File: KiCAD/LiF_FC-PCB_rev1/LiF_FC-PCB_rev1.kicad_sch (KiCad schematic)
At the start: 0 parts

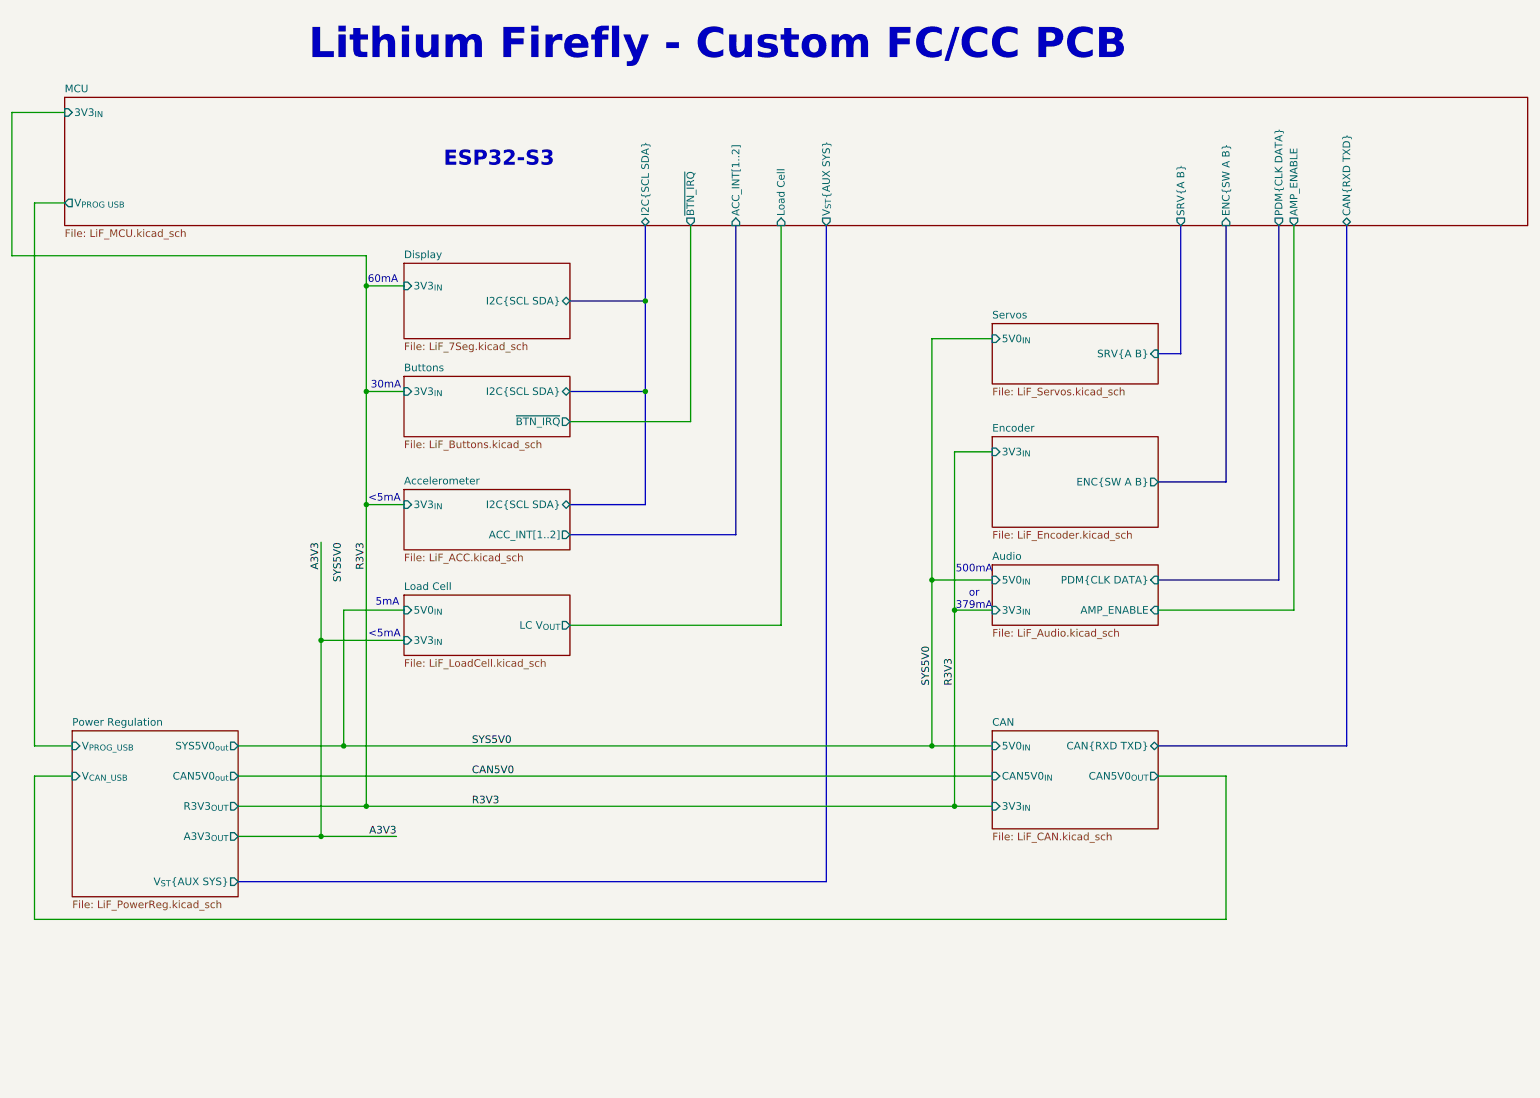
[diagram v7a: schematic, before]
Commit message: added door limit switch and fixed I2C pull up resistors
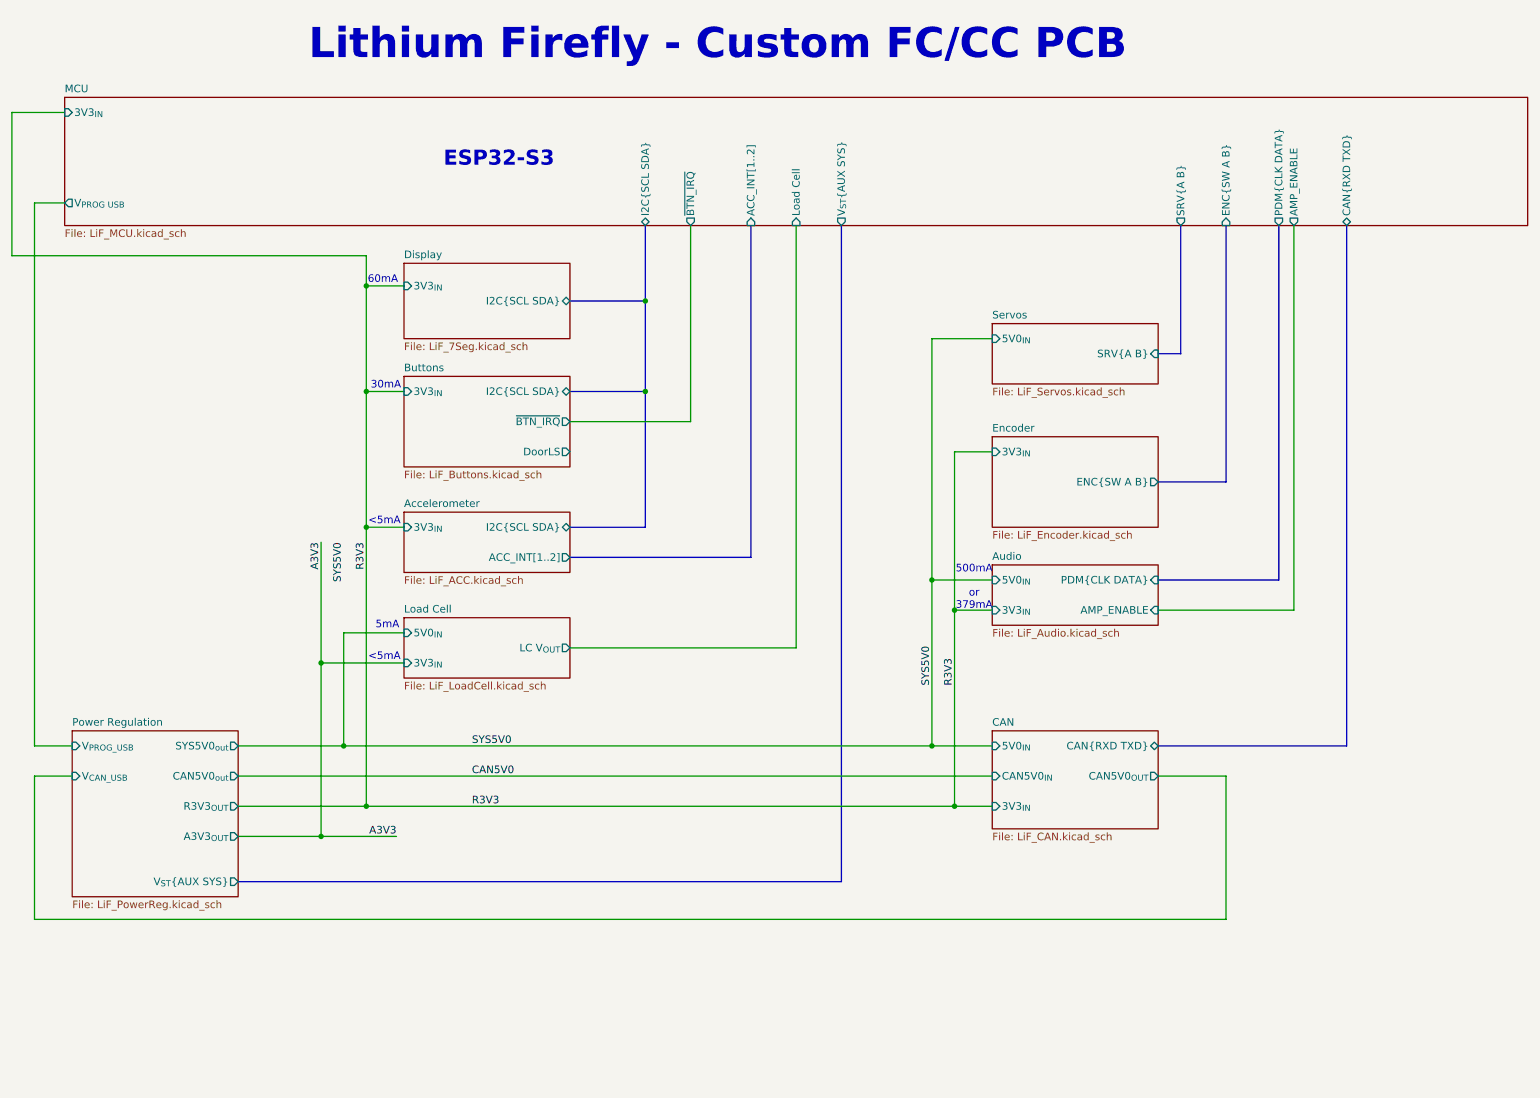
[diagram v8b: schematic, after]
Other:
- sheet Buttons ports: added DoorLS; removed none
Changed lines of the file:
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@@
 	(text "<5mA"
 		(exclude_from_sim no)
-		(at 77.978 94.234 0)
+		(at 77.978 98.044 0)
 		(effects
 			(font
@@
 	(text "5mA"
 		(exclude_from_sim no)
-		(at 78.486 111.76 0)
+		(at 78.486 115.57 0)
 		(effects
 			(font
@@
 	(text "<5mA"
 		(exclude_from_sim no)
-		(at 77.978 117.094 0)
+		(at 77.978 120.904 0)
 		(effects
 			(font
@@
 	)
 	(junction
-		(at 67.31 118.11)
+		(at 74.93 99.06)
 		(diameter 0)
 		(color 0 0 0 0)
@@
 	)
 	(junction
-		(at 74.93 95.25)
-		(diameter 0)
-		(color 0 0 0 0)
-	)
-	(junction
 		(at 67.31 151.13)
 		(diameter 0)
@@
 		(color 0 0 0 0)
 	)
-	(wire
-		(pts
-			(xy 144.78 115.57) (xy 109.22 115.57)
+	(junction
+		(at 67.31 121.92)
+		(diameter 0)
+		(color 0 0 0 0)
+	)
+	(wire
+		(pts
+			(xy 147.32 119.38) (xy 109.22 119.38)
 		)
 		(stroke
@@
 		)
 	)
-	(wire
-		(pts
-			(xy 74.93 95.25) (xy 74.93 146.05)
-		)
-		(stroke
-			(width 0)
-			(type default)
-		)
-	)
 	(bus
 		(pts
@@
 	(bus
 		(pts
-			(xy 137.16 48.26) (xy 137.16 100.33)
-		)
-		(stroke
-			(width 0)
-			(type default)
-		)
-	)
-	(wire
-		(pts
-			(xy 74.93 95.25) (xy 81.28 95.25)
-		)
-		(stroke
-			(width 0)
-			(type default)
-		)
-	)
-	(bus
-		(pts
-			(xy 109.22 95.25) (xy 121.92 95.25)
-		)
-		(stroke
-			(width 0)
-			(type default)
-		)
-	)
-	(wire
-		(pts
-			(xy 74.93 76.2) (xy 74.93 95.25)
+			(xy 139.7 48.26) (xy 139.7 104.14)
+		)
+		(stroke
+			(width 0)
+			(type default)
+		)
+	)
+	(wire
+		(pts
+			(xy 74.93 99.06) (xy 81.28 99.06)
+		)
+		(stroke
+			(width 0)
+			(type default)
+		)
+	)
+	(bus
+		(pts
+			(xy 109.22 99.06) (xy 121.92 99.06)
 		)
 		(stroke
@@
 	(bus
 		(pts
-			(xy 152.4 158.75) (xy 53.34 158.75)
+			(xy 154.94 158.75) (xy 53.34 158.75)
 		)
 		(stroke
@@
 	(wire
 		(pts
-			(xy 71.12 113.03) (xy 81.28 113.03)
+			(xy 71.12 116.84) (xy 81.28 116.84)
 		)
 		(stroke
@@
 	(wire
 		(pts
-			(xy 144.78 48.26) (xy 144.78 115.57)
-		)
-		(stroke
-			(width 0)
-			(type default)
-		)
-	)
-	(bus
-		(pts
-			(xy 137.16 100.33) (xy 109.22 100.33)
+			(xy 147.32 48.26) (xy 147.32 119.38)
+		)
+		(stroke
+			(width 0)
+			(type default)
+		)
+	)
+	(bus
+		(pts
+			(xy 139.7 104.14) (xy 109.22 104.14)
 		)
 		(stroke
@@
 	(wire
 		(pts
-			(xy 67.31 118.11) (xy 67.31 151.13)
+			(xy 74.93 99.06) (xy 74.93 146.05)
 		)
 		(stroke
@@
 		)
 	)
+	(wire
+		(pts
+			(xy 74.93 76.2) (xy 74.93 99.06)
+		)
+		(stroke
+			(width 0)
+			(type default)
+		)
+	)
 	(bus
 		(pts
@@
 	(wire
 		(pts
-			(xy 67.31 101.6) (xy 67.31 118.11)
+			(xy 67.31 101.6) (xy 67.31 121.92)
 		)
 		(stroke
@@
 		)
 	)
+	(wire
+		(pts
+			(xy 67.31 121.92) (xy 67.31 151.13)
+		)
+		(stroke
+			(width 0)
+			(type default)
+		)
+	)
 	(bus
 		(pts
@@
 	(bus
 		(pts
-			(xy 152.4 48.26) (xy 152.4 158.75)
-		)
-		(stroke
-			(width 0)
-			(type default)
-		)
-	)
-	(bus
-		(pts
-			(xy 121.92 95.25) (xy 121.92 76.2)
-		)
-		(stroke
-			(width 0)
-			(type default)
-		)
-	)
-	(wire
-		(pts
-			(xy 67.31 118.11) (xy 81.28 118.11)
+			(xy 154.94 48.26) (xy 154.94 158.75)
+		)
+		(stroke
+			(width 0)
+			(type default)
+		)
+	)
+	(bus
+		(pts
+			(xy 121.92 99.06) (xy 121.92 76.2)
+		)
+		(stroke
+			(width 0)
+			(type default)
+		)
+	)
+	(wire
+		(pts
+			(xy 67.31 121.92) (xy 81.28 121.92)
 		)
 		(stroke
@@
 	(wire
 		(pts
-			(xy 71.12 113.03) (xy 71.12 135.89)
+			(xy 71.12 116.84) (xy 71.12 135.89)
 		)
 		(stroke
@@
 	)
 	(sheet
-		(at 81.28 110.49)
+		(at 81.28 114.3)
 		(size 27.94 10.16)
 		(exclude_from_sim no)
@@
 		)
 		(property "Sheetname" "Load Cell"
-			(at 81.28 109.7784 0)
+			(at 81.28 113.5884 0)
 			(effects
 				(font
@@
 		)
 		(property "Sheetfile" "LiF_LoadCell.kicad_sch"
-			(at 81.28 121.2346 0)
+			(at 81.28 125.0446 0)
 			(effects
 				(font
@@
 		)
 		(pin "3V3_{IN}" input
-			(at 81.28 118.11 180)
+			(at 81.28 121.92 180)
 			(effects
 				(font
@@
 		)
 		(pin "5V0_{IN}" input
-			(at 81.28 113.03 180)
+			(at 81.28 116.84 180)
 			(effects
 				(font
@@
 		)
 		(pin "LC V_{OUT}" output
-			(at 109.22 115.57 0)
+			(at 109.22 119.38 0)
 			(effects
 				(font
@@
 	)
 	(sheet
-		(at 81.28 92.71)
+		(at 81.28 96.52)
 		(size 27.94 10.16)
 		(exclude_from_sim no)
@@
 		)
 		(property "Sheetname" "Accelerometer"
-			(at 81.28 91.9984 0)
+			(at 81.28 95.8084 0)
 			(effects
 				(font
@@
 		)
 		(property "Sheetfile" "LiF_ACC.kicad_sch"
-			(at 81.28 103.4546 0)
+			(at 81.28 107.2646 0)
 			(effects
 				(font
@@
 		)
 		(pin "3V3_{IN}" input
-			(at 81.28 95.25 180)
+			(at 81.28 99.06 180)
 			(effects
 				(font
@@
 		)
 		(pin "ACC_INT[1..2]" output
-			(at 109.22 100.33 0)
+			(at 109.22 104.14 0)
 			(effects
 				(font
@@
 		)
 		(pin "I2C{SCL SDA}" bidirectional
-			(at 109.22 95.25 0)
+			(at 109.22 99.06 0)
 			(effects
 				(font
@@
 	(sheet
 		(at 81.28 73.66)
-		(size 27.94 10.16)
+		(size 27.94 15.24)
 		(exclude_from_sim no)
 		(in_bom yes)
@@
 		)
 		(property "Sheetfile" "LiF_Buttons.kicad_sch"
-			(at 81.28 84.4046 0)
+			(at 81.28 89.4846 0)
 			(effects
 				(font
@@
 		(pin "~{BTN_IRQ}" output
 			(at 109.22 81.28 0)
+			(effects
+				(font
+					(size 1.27 1.27)
+				)
+				(justify right)
+			)
+		)
+		(pin "DoorLS" output
+			(at 109.22 86.36 0)
 			(effects
 				(font
@@
 		)
 		(pin "ACC_INT[1..2]" input
-			(at 137.16 48.26 270)
+			(at 139.7 48.26 270)
 			(effects
 				(font
@@
 		)
 		(pin "Load Cell" input
-			(at 144.78 48.26 270)
+			(at 147.32 48.26 270)
 			(effects
 				(font
@@
 		)
 		(pin "V_{ST}{AUX SYS}" output
-			(at 152.4 48.26 270)
-			(effects
-				(font
+			(at 154.94 48.26 270)
+			(effects
+				(font
